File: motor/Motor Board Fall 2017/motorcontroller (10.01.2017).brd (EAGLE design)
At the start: 76.2 x 50.8 mm, 46 parts, among them CON4 MOLEX_5566-2, CON5 S3B-PH-SM4-TB, CON6 S3B-PH-SM4-TB, U1 TEENSY_3.1_BASIC_2, U2 PCA9685PW, U4 TCAN1042HVDR

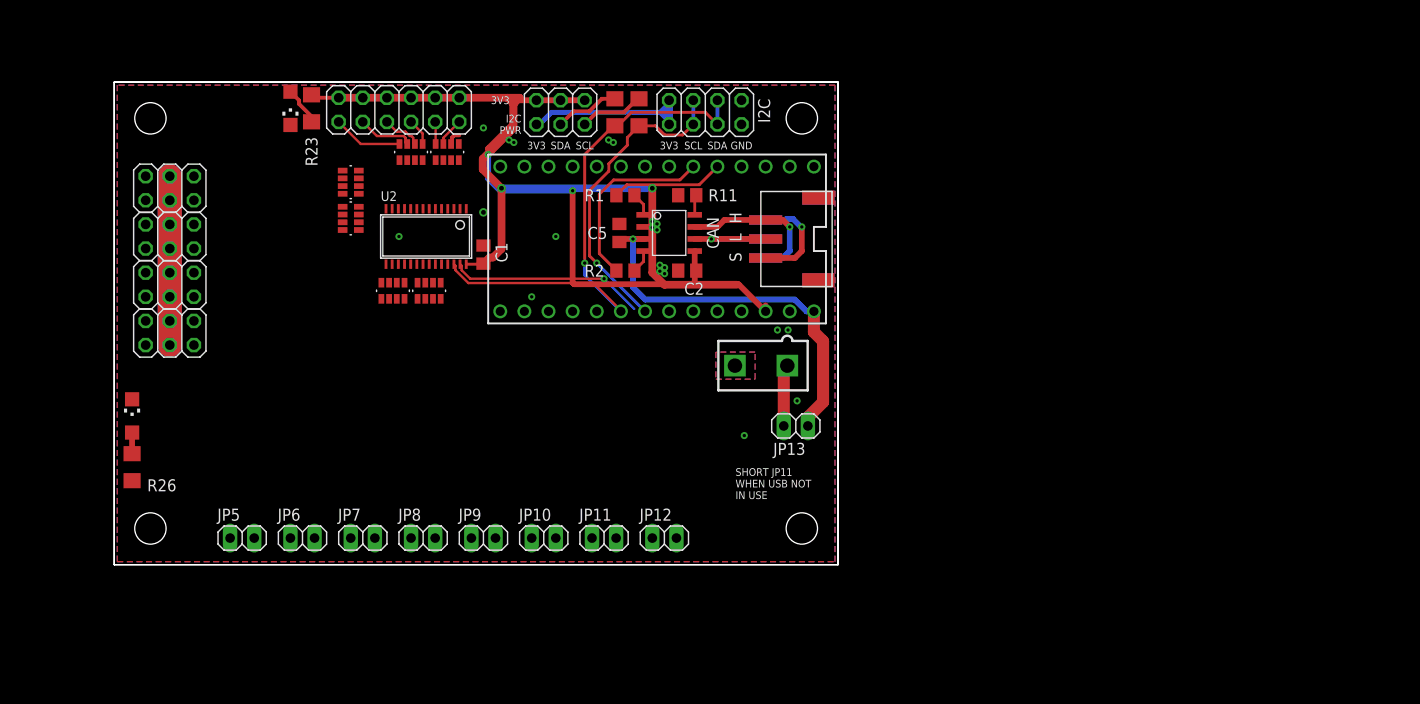
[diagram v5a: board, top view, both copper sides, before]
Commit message: Changed Layout; Reduced size to 2x2 inches
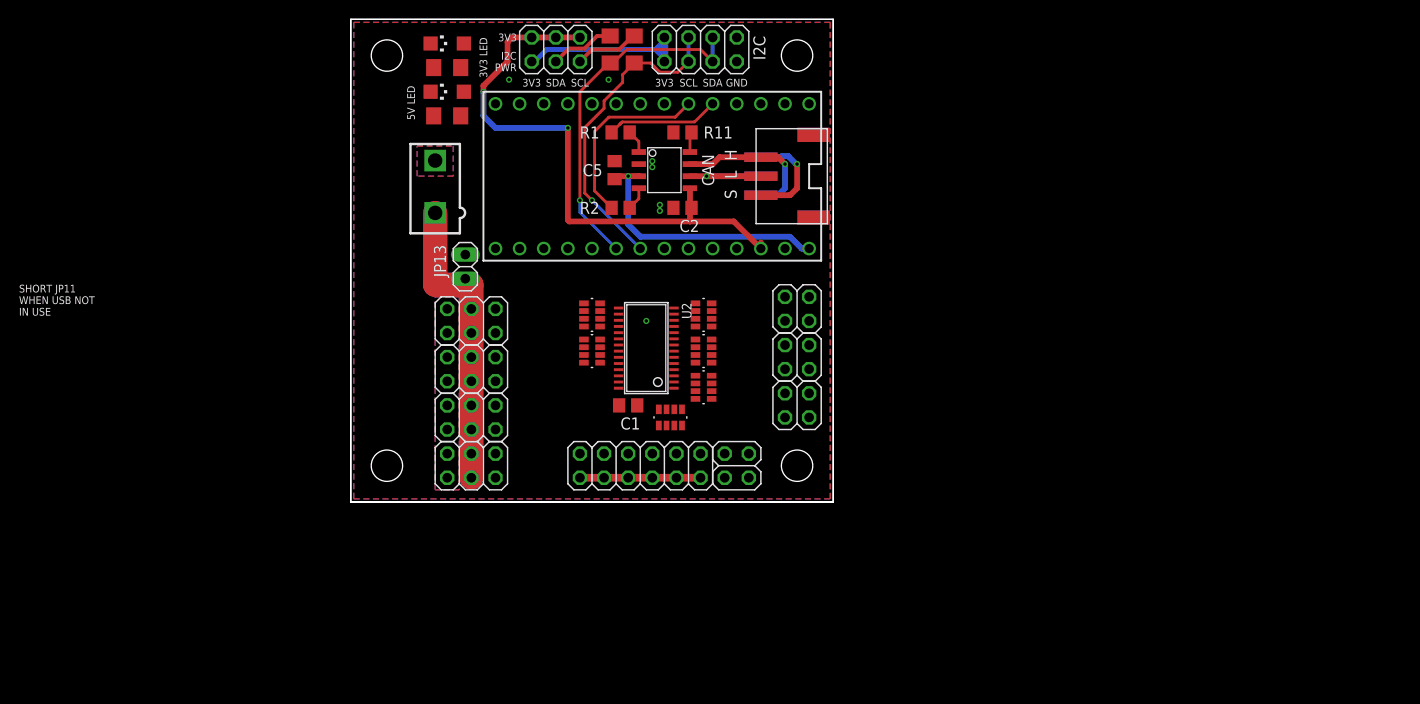
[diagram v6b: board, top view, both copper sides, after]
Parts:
- removed JP10, JP11, JP12, JP5, JP6, JP7, JP8, JP9: (no value), pinhead:1X02
- added JP1, JP15, JP2, JP3: (no value), pinhead:2X02
- moved R26 49.7 mm to (118.1, 119.4), turned to 0 degrees
- moved LED2 47.6 mm to (118.1, 121.9), turned to 90 degrees
- moved JP20 45.3 mm to (138.4, 82.5), turned to 0 degrees
- moved R5 41.2 mm to (145.1, 94.6), turned to 180 degrees
- moved R10 39.5 mm to (145.1, 90.8), turned to 180 degrees
- moved CON4 39.1 mm to (116.8, 111.9), turned to 0 degrees
- moved JP13 38.6 mm to (120.0, 103.5), turned to 270 degrees
- moved R6 38.5 mm to (145.1, 98.4), turned to 180 degrees
- moved R9 36.5 mm to (141.6, 87.6), turned to 90 degrees
- moved JP22 34.7 mm to (120.7, 92.7)
- moved JP21 34.7 mm to (120.7, 97.8)
- moved JP23 34.7 mm to (120.7, 87.6)
- moved JP24 34.7 mm to (120.7, 82.5)
- moved U2 26.0 mm to (139.1, 94.9), turned to 90 degrees
- moved U$4 25.8 mm to (111.8, 125.7)
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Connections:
- net GND: now also JP1.1, JP1.2, JP15.1, JP15.2, JP2.1, JP2.2, JP3.1, JP3.2; no longer JP10.2, JP11.2, JP12.2, JP5.2, JP6.2, JP7.2, JP8.2, JP9.2
- net PWM_ESC0: now also JP1.3, R5.1; no longer JP5.1, R7.1
- net PWM_ESC1: now also JP1.4, R5.2; no longer JP6.1, R7.2
- net PWM_ESC2: now also JP2.3, R5.3; no longer JP7.1, R7.3
- net PWM_ESC3: now also JP2.4, R5.4; no longer JP8.1, R7.4
- net PWM_ESC4: now also JP3.3, R6.1; no longer JP9.1, R8.1
- net PWM_ESC5: now also JP3.4, R6.2; no longer JP10.1, R8.2
- net PWM_ESC6: now also JP15.3, R6.3; no longer JP11.1, R8.3
- net PWM_ESC7: now also JP15.4, R6.4; no longer JP12.1, R8.4
- net PWM_SERVO0: now also R7.1; no longer R5.1
- net PWM_SERVO1: now also R7.2; no longer R5.2
- net PWM_SERVO2: now also R7.3; no longer R5.3
- net PWM_SERVO3: now also R7.4; no longer R5.4
- net PWM_SERVO4: now also R8.1; no longer R6.1
- net PWM_SERVO5: now also R8.2; no longer R6.2
- net PWM_SERVO6: now also R8.3; no longer R6.3
- net PWM_SERVO7: now also R8.4; no longer R6.4
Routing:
- net +3V3: track 142.2 -> 74.4 mm, vias 4 -> 2
- net +5V: track 42.1 -> 63.4 mm
- net SDA: track 57.5 -> 37.0 mm, vias 2 -> 1
- net SCL: track 52.4 -> 33.2 mm
- net VIN: track 41.2 -> 28.1 mm
- net A5: track 7.36 -> 0.00 mm
- net A4+1: track 5.91 -> 0.00 mm
- net A3+1: track 4.18 -> 0.00 mm
- net N$1: track 4.09 -> 0.00 mm
- net A0+1: track 3.02 -> 0.00 mm
- net A2+1: track 2.83 -> 0.00 mm
- net A1+1: track 2.35 -> 0.00 mm
- net N$2: track 2.23 -> 0.00 mm
- net GND: track 1.58 -> 0.00 mm, vias 21 -> 7
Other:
- board size 76.2 x 50.8 mm -> 50.8 x 50.8 mm
- board text added: "3V3 LED"
- board text added: "5V LED"

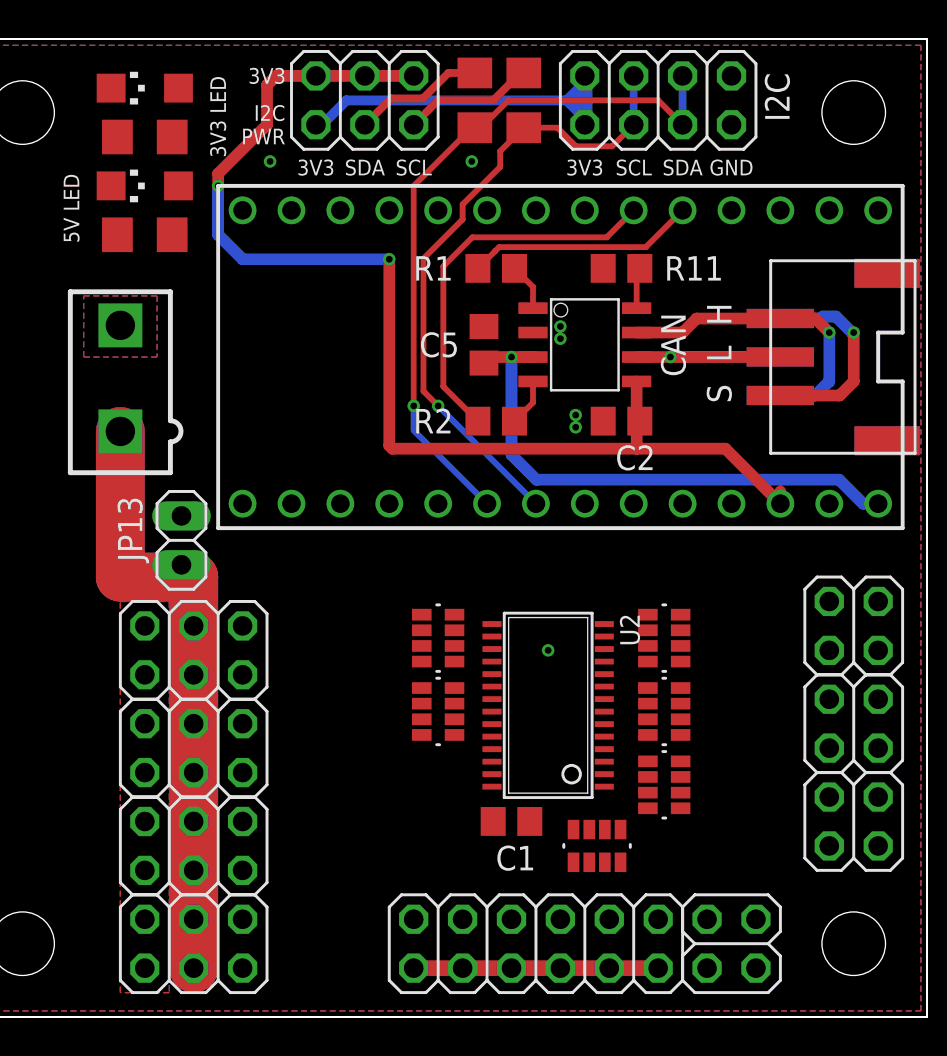
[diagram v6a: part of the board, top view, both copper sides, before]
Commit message: Routed most components
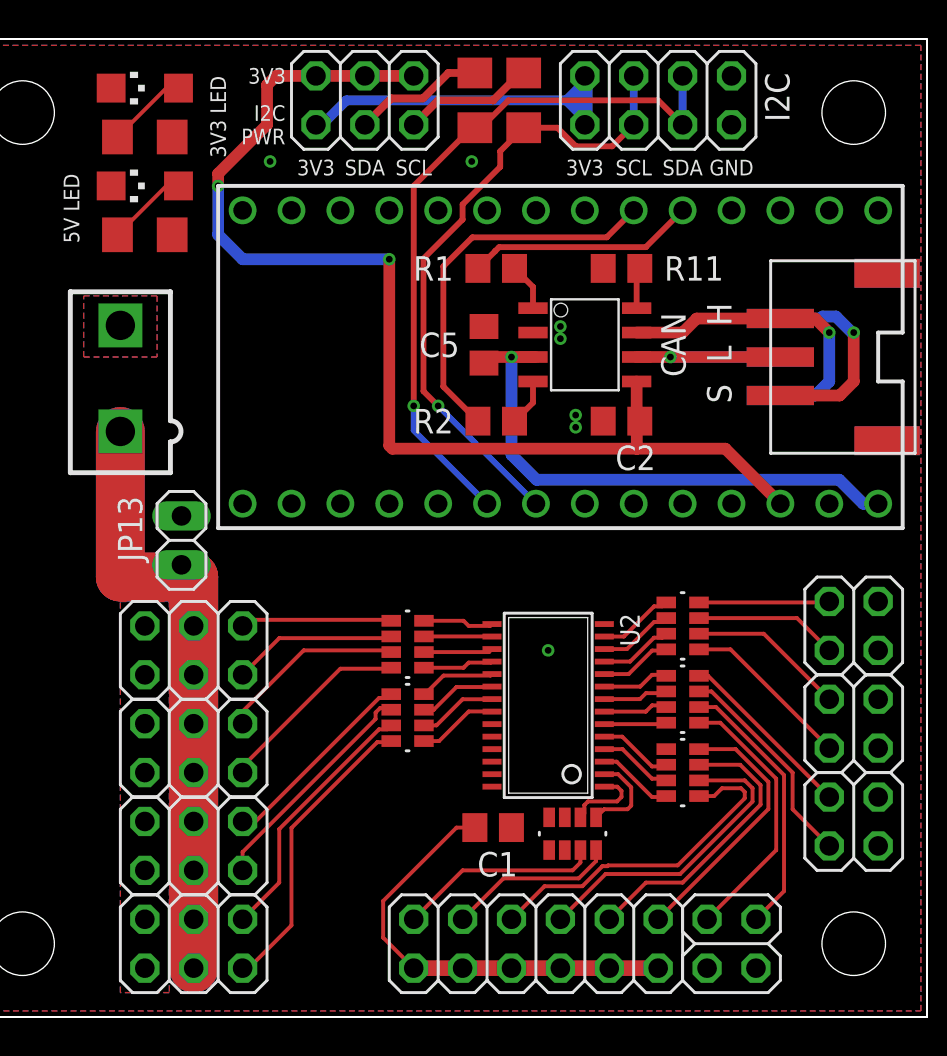
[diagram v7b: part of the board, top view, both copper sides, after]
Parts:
- moved R7 1.62 mm to (131.8, 98.1)
- moved R8 1.62 mm to (131.8, 94.3)
- moved R9 1.42 mm to (140.3, 88.3)
- moved R5 1.14 mm to (146.1, 95.2)
- moved R6 1.14 mm to (146.1, 99.1)
- moved R10 1.14 mm to (146.1, 91.4)
- moved C1 1.00 mm to (136.2, 88.6)
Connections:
- net PWM_ESC0: now also JP15.4; no longer JP1.3
- net PWM_ESC1: now also JP15.3; no longer JP1.4
- net PWM_ESC2: now also JP1.4; no longer JP2.3
- net PWM_ESC3: now also JP1.3; no longer JP2.4
- net PWM_ESC4: now also JP2.4; no longer JP3.3
- net PWM_ESC5: now also JP2.3; no longer JP3.4
- net PWM_ESC6: now also JP3.4; no longer JP15.3
- net PWM_ESC7: now also JP3.3; no longer JP15.4
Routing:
- net A2+1: track 0.00 -> 17.7 mm
- net A3+1: track 0.00 -> 16.2 mm
- net PWM_SERVO7: track 0.00 -> 15.6 mm
- net A4+1: track 0.00 -> 15.0 mm
- net PWM_ESC0: track 0.00 -> 14.0 mm
- net PWM_ESC1: track 0.00 -> 14.0 mm
- net A5: track 0.00 -> 13.8 mm
- net PWM_SERVO6: track 0.00 -> 13.5 mm
- net PWM_SERVO5: track 0.00 -> 12.0 mm
- net PWM_ESC2: track 0.00 -> 11.2 mm
- net A0+1: track 0.00 -> 10.5 mm
- net PWM_SERVO4: track 0.00 -> 10.5 mm
- net PWM_SERVO3: track 0.00 -> 10.2 mm
- net +3V3: track 74.4 -> 84.3 mm
- net PWM_SERVO2: track 0.00 -> 9.71 mm
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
